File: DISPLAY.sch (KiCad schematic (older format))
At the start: 36 parts, among them P301 SEPS525, U301 TPS61041DBV

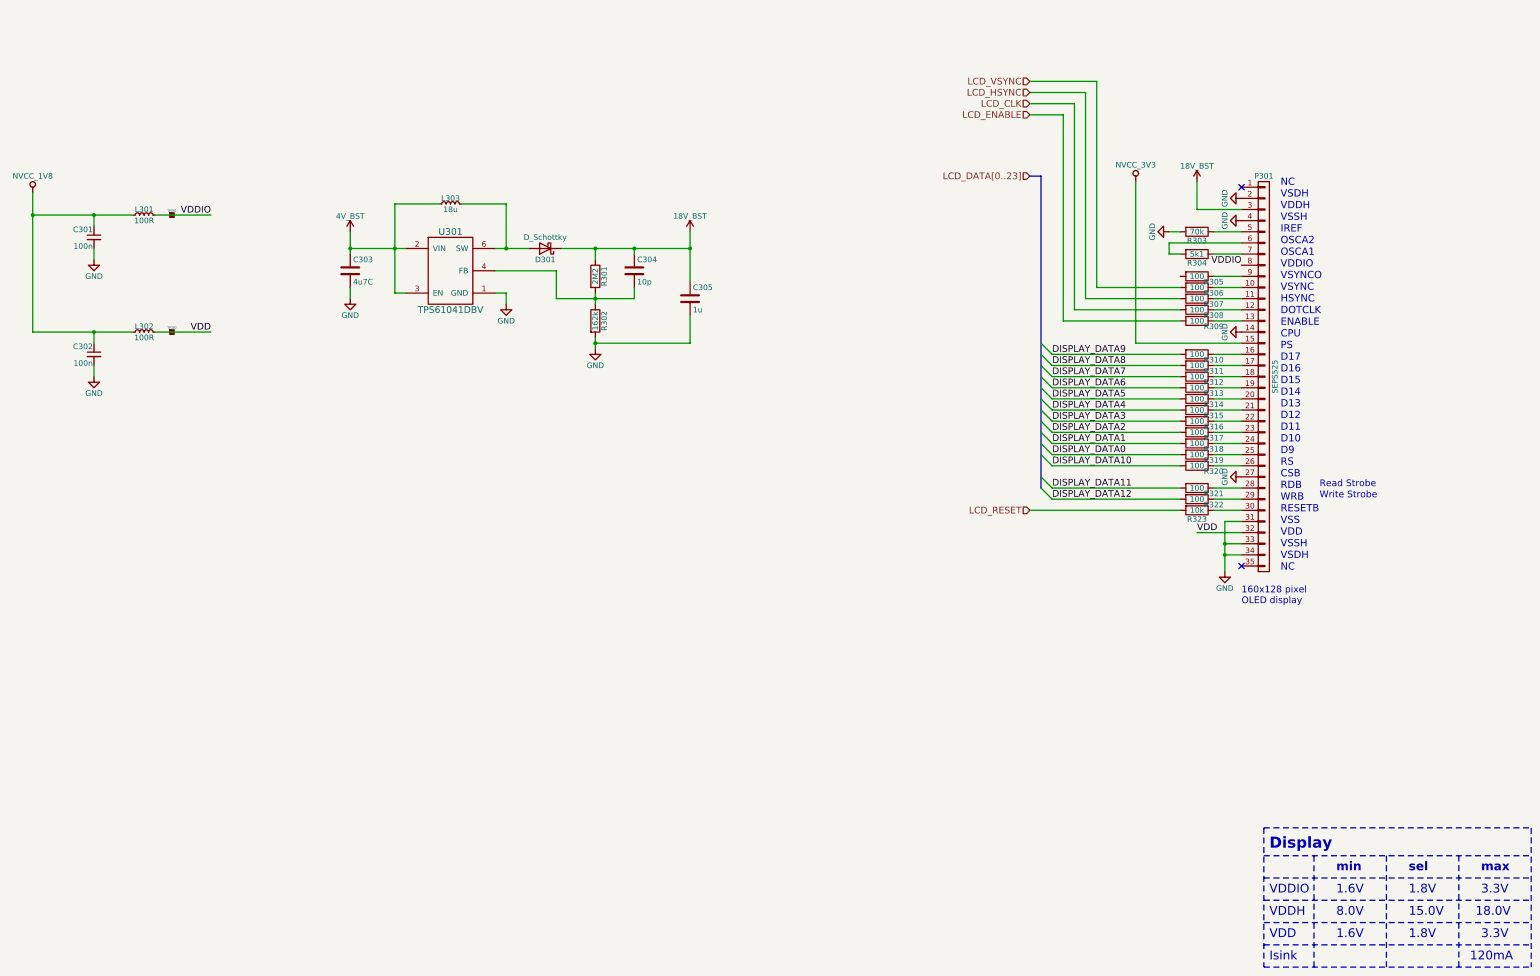
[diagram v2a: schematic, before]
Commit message: This branch moves from i.mx7 to STM32F4 CPU to be finished for Hackaday Prize 2017
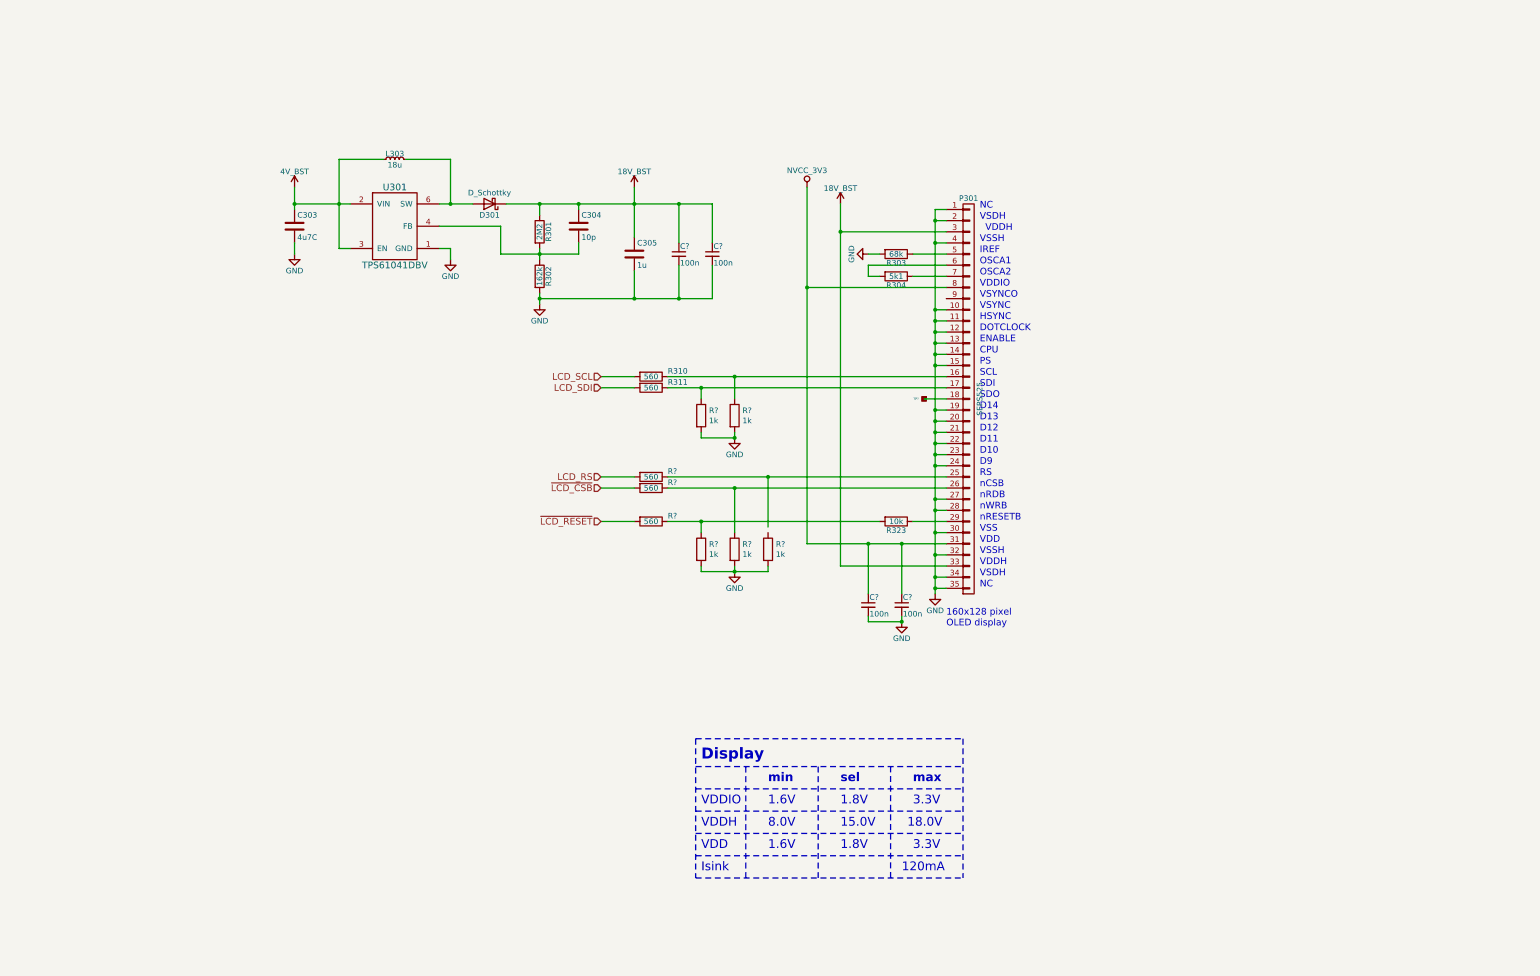
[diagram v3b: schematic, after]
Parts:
- removed C301, C302: 100n, Capacitors_SMD:C_0402, symbol C_Small
- removed L301, L302: 100R, Choke_SMD:Choke_SMD_1206_Standard, symbol L_Small
- removed R305, R306, R307, R308, R309, R312, R313, R314, R315, R316, R317, R318, R319, R320, R321, R322: 100, Resistors_SMD:R_0402, symbol R
- removed TP301, TP302: TP, NokiaRetroFit:TP, symbol TP
- added C? (x4): 100n, Capacitors_SMD:C_0402, symbol C_Small
- added R? (x5): 1k, symbol R
- added R? (x3): 560, Resistors_SMD:R_0402, symbol R
- added TP?: TP, symbol TP
- R303: value 70k -> 68k
- R310, R311: value 100 -> 560
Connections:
- net VDD is gone; now on net GND: P301.32 (P32)
- net VDDIO is gone; now on net NVCC_3V3: P301.8 (P8)
- net 18V_BST: now also P301.33 (P33), C?.1, C?.1
- net GND: now also P301.1 (P1), P301.10 (P10), P301.11 (P11), P301.12 (P12), P301.13 (P13), P301.15 (P15), P301.19 (P19), P301.20 (P20), P301.21 (P21), P301.22 (P22), P301.23 (P23), P301.24 (P24), P301.28 (P28), P301.30 (P30), P301.35 (P35), C?.2, C?.2, C?.2, C?.2, R?.2, R?.2, R?.2, R?.2, R?.2; no longer P301.31 (P31), P301.33 (P33)
- net NVCC_3V3: now also P301.31 (P31), C?.1, C?.1; no longer P301.15 (P15)
- net at P301.16 (P16), R310.1: now also R?.1
- net at P301.17 (P17), R311.1: now also R?.1
- net at P301.18 (P18): now also TP?.1
- net at P301.25 (P25): now also R?.1
- net at P301.26 (P26): now also R?.1, R?.1
- net at P301.29 (P29): now also R323.1
- net DISPLAY_DATA8 renamed LCD_SDI
- net DISPLAY_DATA9 renamed LCD_SCL
- net LCD_RESET: no longer names the net of R323.2
- net LCD_RESET: now also R?.1, R?.1
- new net LCD_RS: R?.2
- new net ~LCD_CSB: R?.2
- new net ~LCD_RESET: R?.2
- no-connect marks 2 -> 0
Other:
- note added: "CPU"
- note added: "D10"
- note added: "D11"
- note added: "D12"
- note added: "D13"
- note added: "D14"
- note added: "D9"
- note added: "DOTCLOCK"
- note added: "ENABLE"
- note added: "HSYNC"
- note added: "IREF"
- note added: "NC"
- note added: "OSCA1"
- note added: "OSCA2"
- note added: "PS"
- note added: "RS"
- note added: "SCL"
- note added: "SDI"
- note added: "SDO"
- note added: "VSDH"
- note added: "VSS"
- note added: "VSSH"
- note added: "VSYNC"
- note added: "VSYNCO"
- note added: "nCSB"
- note added: "nRDB"
- note added: "nRESETB"
- note added: "nWRB"
- note removed: "NC\nVSDH\nVDDH\nVSSH\nIREF\nOSCA2\nOSCA1\nVDDIO\nVSYNCO\nVSYNC\nHSYNC\nDOTCLK\nENABLE\nCPU\nPS\nD17\nD16\nD15\nD14\nD13\nD12\nD11\nD10\nD9\nRS\nCSB\nRDB\nWRB\nRESETB\nVSS\nVDD\nVSSH\nVSDH\nNC"
- note removed: "Read Strobe"
- note removed: "Write Strobe"
- moved on the sheet: C303, C304, C305, D301, L303, P301, R301, R302, R303, R304, R310, R311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

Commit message: Modification for STM32 adaption
For the Hackaday Prize 2017 I decided to switch to STM32 as CPU

*Power system was modified to just contain the charge IC,
*Boost converter for high voltage peripherals
*Buck converter for 3V3 for CPU and switchable NVCC_3V3
   for peripherie

CPU signals are routed and pinmux is done in firmware folder.

SD-Card has 4bit Interface

WiFi module ESP8266 is connected via UART

Wolfson Ausio codec is connected via SAI

Two digital microphones for noise canceling

Rumble Motor driver

LCD is connected via it's own I2C interface
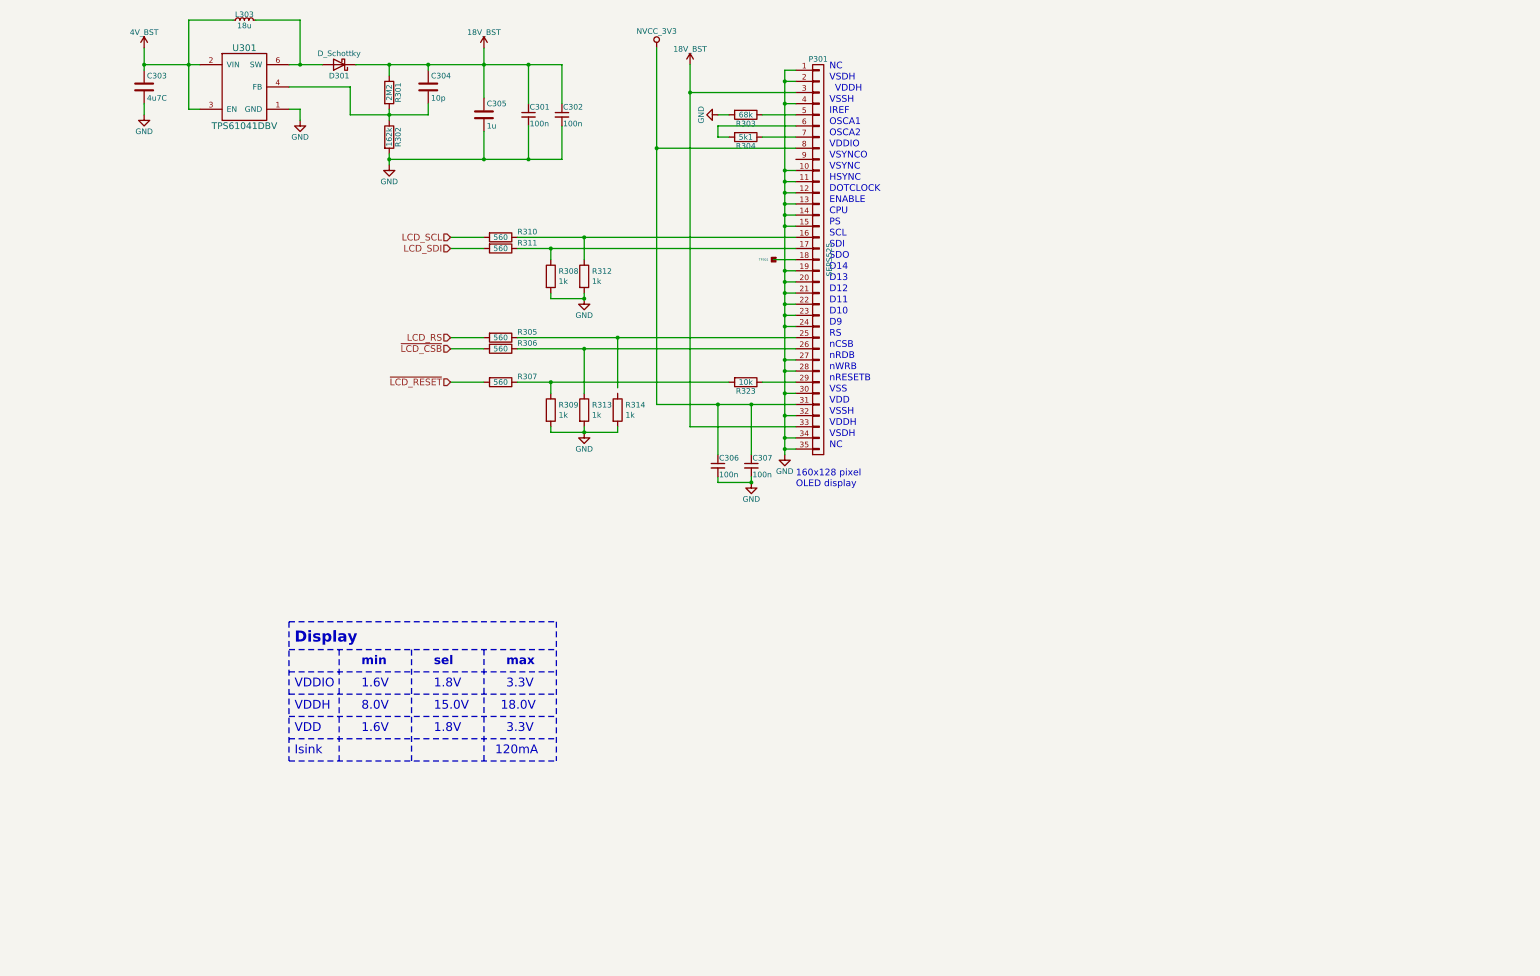
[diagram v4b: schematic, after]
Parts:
- C301, C302, C306, C307: renamed from C?; footprint Capacitors_SMD:C_0402 -> Capacitors_SMD:C_0402_NoSilk
- C303, C305: footprint Capacitors_SMD:C_0603 -> Capacitors_SMD:C_0402_NoSilk
- C304: footprint Capacitors_SMD:C_0402 -> Capacitors_SMD:C_0402_NoSilk
- R301, R302, R303, R304, R310, R311, R323: footprint Resistors_SMD:R_0402 -> Resistors_SMD:R_0402_NoSilk
- R305, R306, R307: renamed from R?; footprint Resistors_SMD:R_0402 -> Resistors_SMD:R_0402_NoSilk
- R308, R309, R312, R313, R314: renamed from R?; footprint (none) -> Resistors_SMD:R_0402_NoSilk
- TP301: renamed from TP?; footprint (none) -> NokiaRetroFit:TP
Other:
- moved on the sheet: C301, C302, C303, C304, C305, C306, C307, D301, L303, P301, R301, R302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

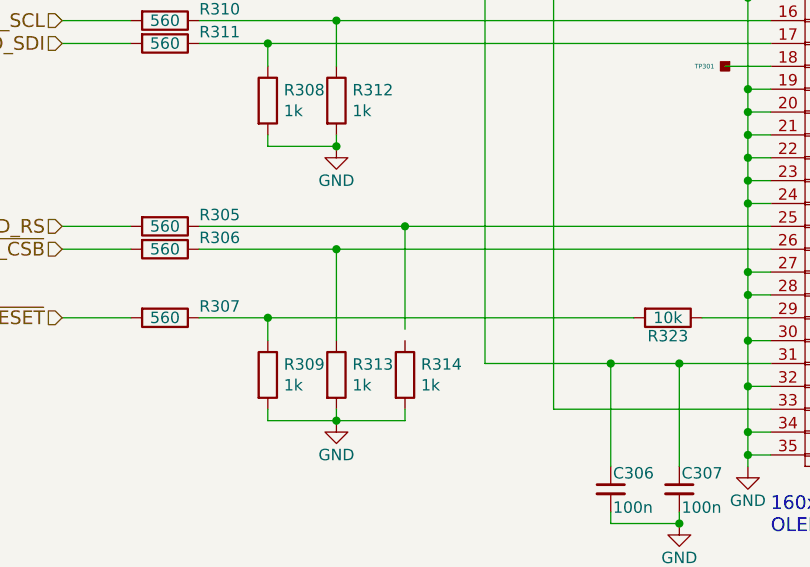
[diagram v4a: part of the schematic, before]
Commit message: Placed a lot of components and routed the audio codec
The BGA of tha audio chipset is to small for regualr technology.
We do not use all of the pins of the chip so we ignore the other
pads and escape throug the balls of the other pad.
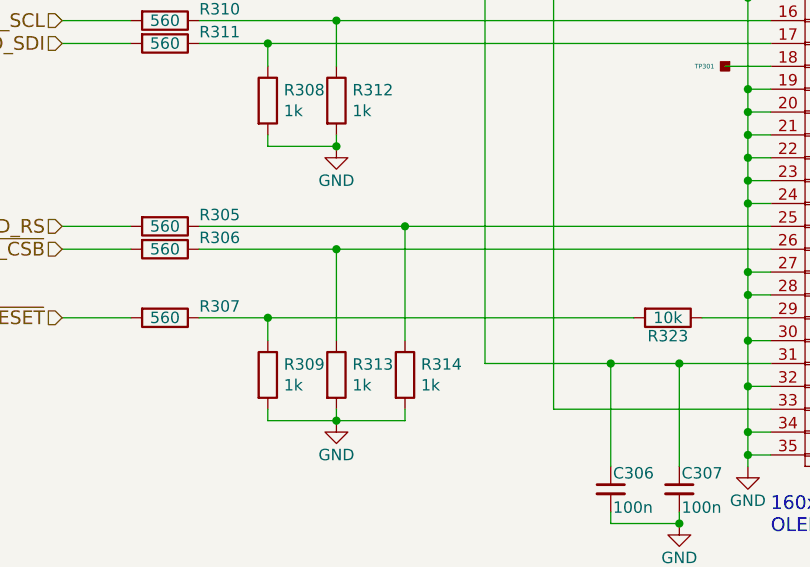
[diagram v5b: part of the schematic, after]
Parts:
- D301: footprint Diodes_SMD:DD-PAK_TO263_SingleDiode -> Diodes_SMD:D_0805
- U301: footprint TO_SOT_Packages_SMD:SOT-23 -> Housings_DFN_QFN:DFN-6-1EP_2x2mm_Pitch0.65mm
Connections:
- net at P301.25 (P25), R305.1: now also R314.1
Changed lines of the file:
@@
 LIBS:contrib
 LIBS:valves
-LIBS:tps62742
-LIBS:WM8994ECS
+LIBS:stm32
 LIBS:3210retro-cache
 EELAYER 26 0
@@
 F 0 "U301" H 4050 2000 60  0000 C CNN
 F 1 "TPS61041DBV" H 4050 1300 60  0000 C CNN
-F 2 "TO_SOT_Packages_SMD:SOT-23" H 4050 1450 60  0001 C CNN
+F 2 "Housings_DFN_QFN:DFN-6-1EP_2x2mm_Pitch0.65mm" H 4050 1450 60  0001 C CNN
 F 3 "" H 4050 1450 60  0001 C CNN
 	1    4050 1650
@@
 F 0 "D301" H 4900 1550 50  0000 C CNN
 F 1 "D_Schottky" H 4900 1350 50  0000 C CNN
-F 2 "Diodes_SMD:DD-PAK_TO263_SingleDiode" H 4900 1450 50  0001 C CNN
+F 2 "Diodes_SMD:D_0805" H 4900 1450 50  0001 C CNN
 F 3 "" H 4900 1450 50  0000 C CNN
 	1    4900 1450
@@
 Connection ~ 7100 4000
 Wire Wire Line
-	7400 4350 7400 3900
+	7400 4400 7400 3900
 Connection ~ 7400 3900
 $Comp
